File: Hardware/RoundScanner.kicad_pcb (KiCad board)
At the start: 4 copper layers, 45 x 42.5 mm, 81 parts, among them J1 I2C ThroughHole, J3 I2C, J4 Interface, Q1 BSS138DW-7-F, U1 OPA2376xxD, U2 NAU7802SGI, U4 OPA2376xxD, U5 TLC59208FIPWR, U6 AS7341-DLGT, U7 AP7312-1833W6-7, X1 SG-8002CE

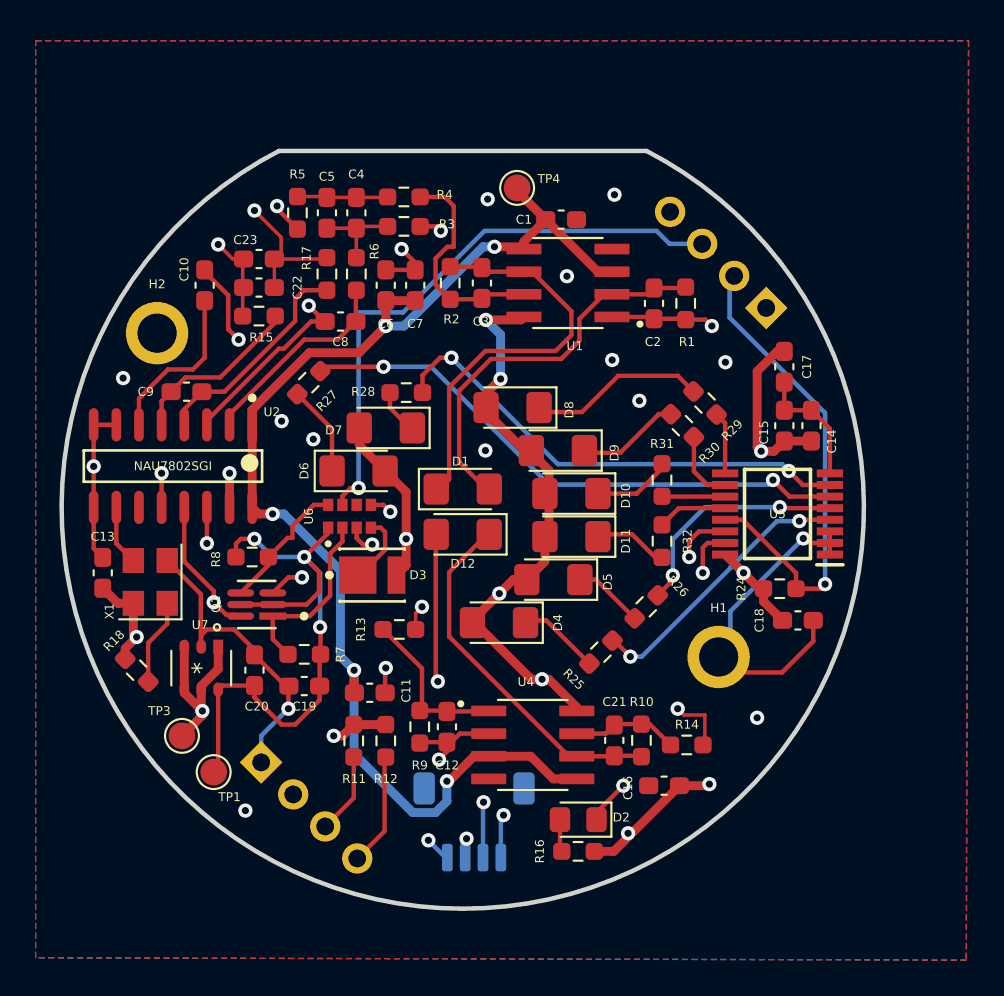
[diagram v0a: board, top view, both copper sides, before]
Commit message: optimized layout, cleaned up some traces, opened up the ground and power inner layers so they're less constrained. changed mounting holes to solid to increase ground plane
verified DRC still passed

Signed-off-by: lokimetasmith <lokimail@gmail.com>
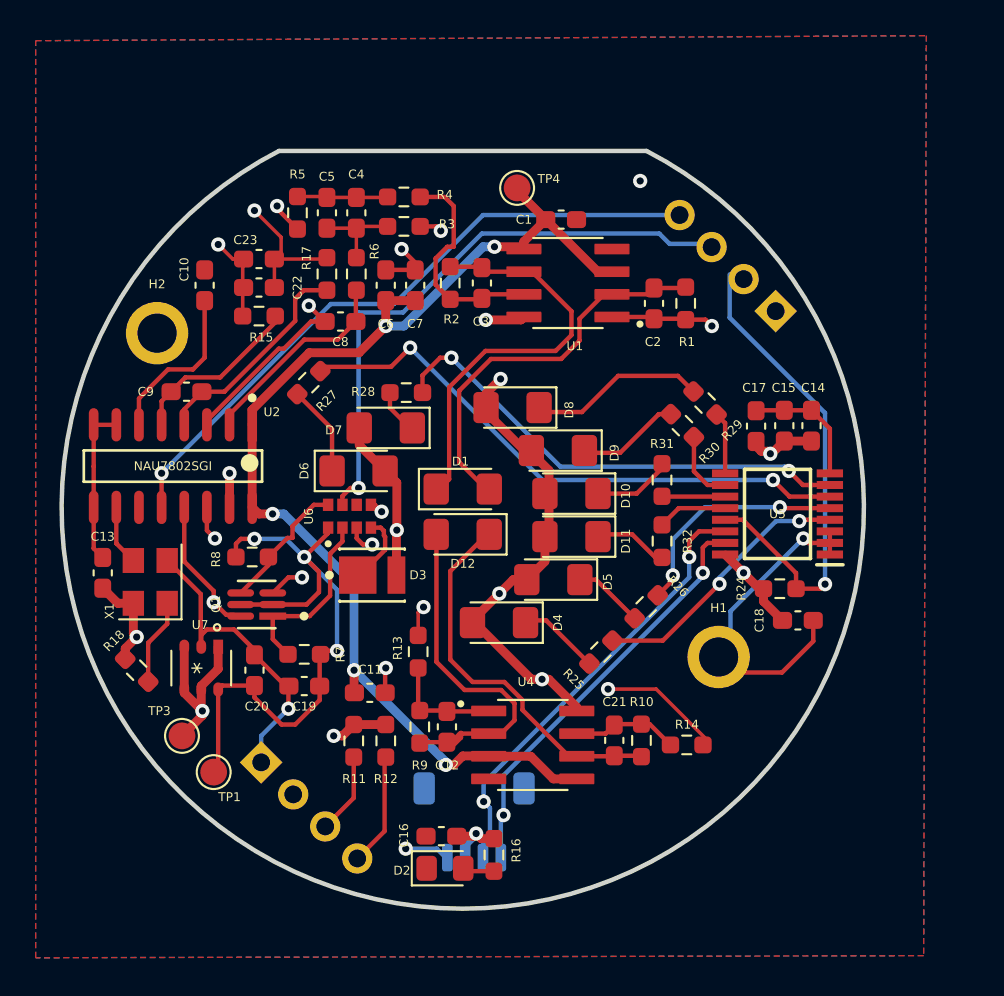
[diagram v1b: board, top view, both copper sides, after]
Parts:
- moved C16 12.8 mm to (88.1, 125.8)
- moved D2 7.96 mm to (88.3, 127.6), turned to 0 degrees
- moved R16 4.72 mm to (91.0, 126.8), turned to -90 degrees
- moved C17 3.69 mm to (105.7, 102.8), turned to 90 degrees
- moved R13 1.63 mm to (86.8, 115.4), turned to 90 degrees
- moved J4 0.56 mm to (106.8, 96.3)
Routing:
- net +3V3: track 94.3 -> 69.6 mm, vias 14 -> 12
- net GND: track 64.1 -> 57.9 mm, vias 22 -> 8
- net +2V5: track 71.6 -> 66.1 mm
- net Net-(C12-Pad2): track 9.12 -> 6.14 mm
- net Net-(C12-Pad1): track 17.7 -> 20.1 mm, vias 2 -> 0
- net +1V8: track 34.6 -> 35.8 mm
- net Net-(C21-Pad1): track 19.8 -> 20.8 mm
- net Net-(R27-Pad1): track 31.6 -> 32.2 mm
- net Net-(R25-Pad1): track 15.7 -> 15.1 mm

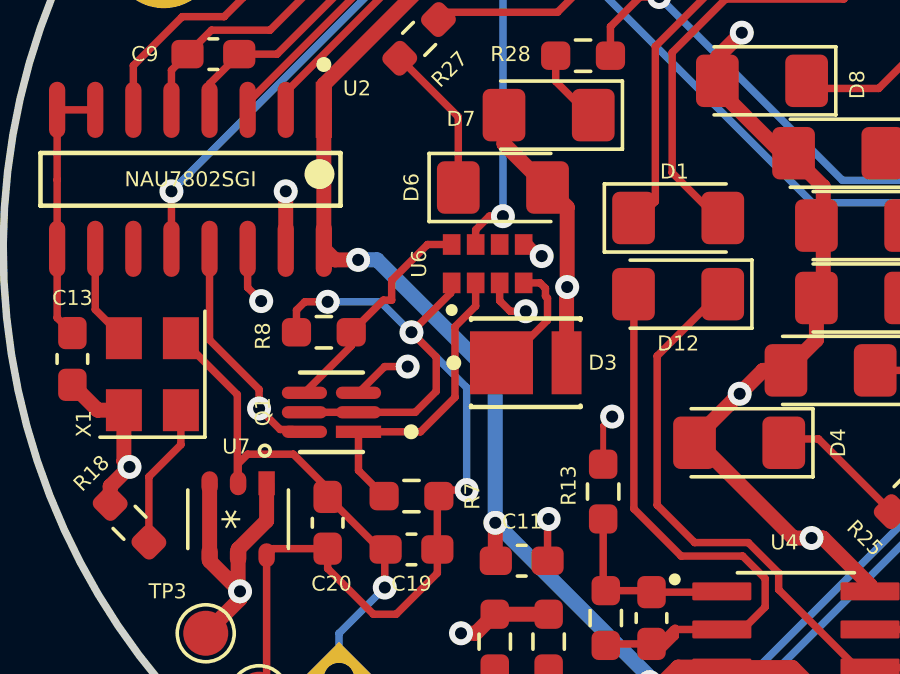
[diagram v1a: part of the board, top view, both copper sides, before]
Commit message: Added pullup resistor to AS7341_INT line
Signed-off-by: lokimetasmith <lokimail@gmail.com>
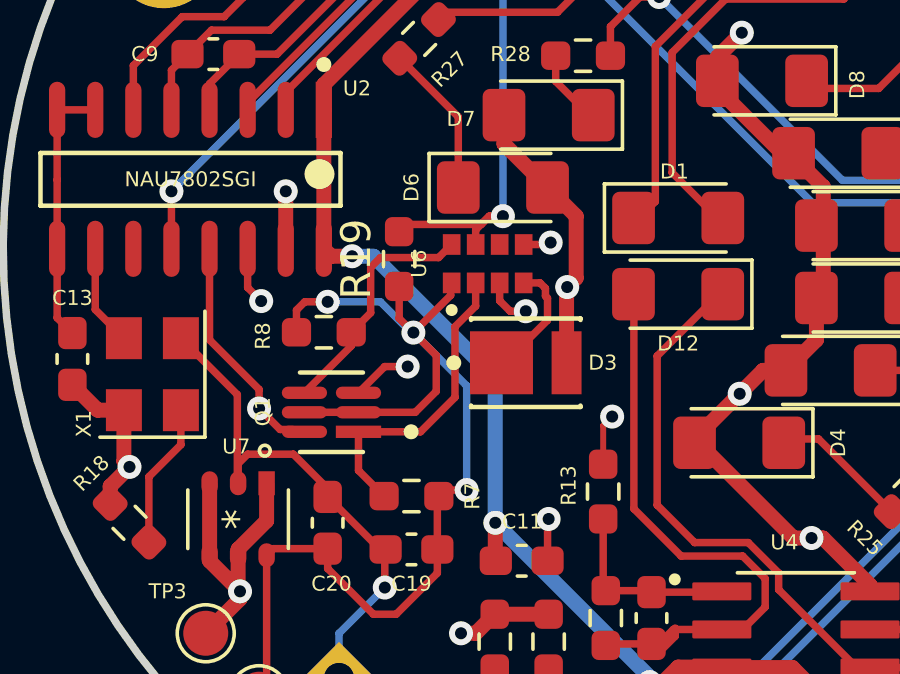
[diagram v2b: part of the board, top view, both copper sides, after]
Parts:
- added R19: 10k, Resistor_SMD:R_0603_1608Metric_Pad0.98x0.95mm_HandSolder, F.Cu at (80.0, 107.7)
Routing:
- net AS7341_INT: track 32.8 -> 36.0 mm
- net +1V8: track 35.8 -> 37.5 mm
